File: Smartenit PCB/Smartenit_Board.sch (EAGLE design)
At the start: 86 parts, among them J3 2X5CONNECTOR1.27MM, Q1 QUARTZ_3.58M_2PIN, U1 ADE7953, U2 ESP-WROOM-32, U3 SN74LVC1G3157

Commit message: renumber board
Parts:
- removed D6: (no value), SparkFun:DIODESMA
- removed R43: 470, Nizanlib:0402-RES
- added D3: 250mA/100V, SparkFun-DiscreteSemi:DIODE-BAS16J
- added R37: 124k, SparkFun-Resistors:100KOHM-0603-1/10W-1%
- C1: value 20p -> 105/25V; device Nizanlib:0402-CAP -> SparkFun-Capacitors:680PF-0603-50V-10%
- C11, C12: value 333n -> 475n
- C14: value 475n -> 333n
- C15: value 104n -> 475n
- C16: value 475n -> 104n
- C17: device resistor:C-EUC0805K -> Nizanlib:0402-CAP
- C18: value 104 -> 333n; device SparkFun-Capacitors:680PF-0603-50V-10% -> Nizanlib:0402-CAP
- C19: value 22uF/6.3V -> 333n; device SparkFun-Capacitors:680PF-0603-50V-10% -> resistor:C-EUC0805K
- C2: value 20p -> 10uF/6.3V; device Nizanlib:0402-CAP -> SparkFun:CAP0603-CAP
- C20: value 104 -> 333n; device SparkFun-Capacitors:680PF-0603-50V-10% -> resistor:C-EUC0805K
- C21: value 150p -> 104; device SparkFun-Capacitors:680PF-0603-50V-10% -> SparkFun:CAP0603-CAP
- C22: value 105/25V -> (none); device SparkFun-Capacitors:680PF-0603-50V-10% -> SparkFun:CAP_POL1206
- C23: value 10uF/6.3V -> 104; device SparkFun:CAP0603-CAP -> SparkFun-Capacitors:680PF-0603-50V-10%
- C24: value 104 -> (none); device Nizanlib:0402-CAP -> SparkFun:CAP_POLPTH1
- C25: device SparkFun:CAP0603-CAP -> SparkFun-Capacitors:680PF-0603-50V-10%
- C26: value (none) -> 150p; device SparkFun:CAP_POLPTH1 -> SparkFun-Capacitors:680PF-0603-50V-10%
- C3: value 104n -> 104
- C4: value 104n -> 333n
- C5: value 333n -> 104n
- C6: value 333n -> 22uF/6.3V; device Nizanlib:0402-CAP -> SparkFun-Capacitors:680PF-0603-50V-10%
- C7: value 333n -> 20p; device resistor:C-EUC0805K -> Nizanlib:0402-CAP
- C8: value 475n -> 20p
- C9: value (none) -> 104n; device SparkFun:CAP_POL1206 -> Nizanlib:0402-CAP
- D1: value 250mA/100V -> (none); device SparkFun-DiscreteSemi:DIODE-BAS16J -> SparkFun:DIODESMA
- R1, R10: value 1k -> 10k; device Nizanlib:0402-RES -> SparkFun-Resistors:100KOHM-0603-1/10W-1%
- R11: value 51 -> 10k; device Nizanlib:0402-RES -> SparkFun-Resistors:100KOHM-0603-1/10W-1%
- R12: value 9.1k -> 4.7k; device Nizanlib:0402-RES -> SparkFun-Resistors:100KOHM-0603-1/10W-1%
- R13: value 100k -> 1k; device SparkFun-Resistors:100KOHM-0603-1/10W-1% -> SparkFun-Resistors:1KOHM-0603-1/10W-1%
- R14, R15: value 100k -> 470; device SparkFun-Resistors:100KOHM-0603-1/10W-1% -> Nizanlib:0402-RES
- R16: value 124k -> 12k; device SparkFun-Resistors:100KOHM-0603-1/10W-1% -> Nizanlib:0402-RES
- R17: value 40.2k -> 1k; device SparkFun-Resistors:100KOHM-0603-1/10W-1% -> Nizanlib:0402-RES
- R18: value 1k -> 9.1k; device resistor:R-EU_ -> Nizanlib:0402-RES
- R19: value 1k -> 51; device resistor:R-EU_ -> Nizanlib:0402-RES
- R2: value 1k -> 56k; device Nizanlib:0402-RES -> SparkFun-Resistors:100KOHM-0603-1/10W-1%
- R20: value 100k -> 51; device SparkFun-Resistors:100KOHM-0603-1/10W-1% -> Nizanlib:0402-RES
- R21: value 10k -> 1k; device SparkFun-Resistors:10KOHM-0603-1/10W-1% -> Nizanlib:0402-RES
- R22: value 9.1k -> 10k
- R23: value 220 -> 1k; device SparkFun-Resistors:10KOHM-0603-1/10W-1% -> resistor:R-EU_
- R24: value 220 -> 1k; device SparkFun-Resistors:10KOHM-0603-1/10W-1% -> Nizanlib:0402-RES
- R25: value 220 -> 9.1k; device SparkFun-Resistors:10KOHM-0603-1/10W-1% -> Nizanlib:0402-RES
- R26: value 10k -> 1k; device SparkFun-Resistors:100KOHM-0603-1/10W-1% -> Nizanlib:0402-RES
- R27: value 4.7k -> 9.1k; device SparkFun-Resistors:100KOHM-0603-1/10W-1% -> Nizanlib:0402-RES
- R28: value 10k -> 9.1k; device SparkFun-Resistors:100KOHM-0603-1/10W-1% -> Nizanlib:0402-RES
- R29: value 4.7k -> 51; device SparkFun-Resistors:100KOHM-0603-1/10W-1% -> Nizanlib:0402-RES
- R3: value 10k -> 200k; device Nizanlib:0402-RES -> SparkFun-Resistors:100KOHM-0603-1/10W-1%
- R30: value 10k -> 51; device SparkFun-Resistors:100KOHM-0603-1/10W-1% -> Nizanlib:0402-RES
- R31: device SparkFun-Resistors:100KOHM-0603-1/10W-1% -> resistor:R-EU_
- R32: value 200k -> 12k; device SparkFun-Resistors:100KOHM-0603-1/10W-1% -> Nizanlib:0402-RES
- R33: value 56k -> 220; device SparkFun-Resistors:100KOHM-0603-1/10W-1% -> SparkFun-Resistors:10KOHM-0603-1/10W-1%
- R34: value 1k -> 100k; device SparkFun-Resistors:1KOHM-0603-1/10W-1% -> SparkFun-Resistors:100KOHM-0603-1/10W-1%
- R35: value 1k -> 40.2k; device SparkFun-Resistors:1KOHM-0603-1/10W-1% -> SparkFun-Resistors:100KOHM-0603-1/10W-1%
- R36, R40: value 12k -> 100k; device Nizanlib:0402-RES -> SparkFun-Resistors:100KOHM-0603-1/10W-1%
- R38: value 470 -> 10k; device Nizanlib:0402-RES -> SparkFun-Resistors:10KOHM-0603-1/10W-1%
- R39: value 470 -> 100k; device Nizanlib:0402-RES -> SparkFun-Resistors:100KOHM-0603-1/10W-1%
- R4: value 9.1k -> 1k; device Nizanlib:0402-RES -> SparkFun-Resistors:1KOHM-0603-1/10W-1%
- R41: value 470 -> 220; device Nizanlib:0402-RES -> SparkFun-Resistors:10KOHM-0603-1/10W-1%
- R42: value 12k -> 220; device Nizanlib:0402-RES -> SparkFun-Resistors:10KOHM-0603-1/10W-1%
- R5: value 51 -> 470
- R6: value 51 -> 12k
- R7: value 9.1k -> 470
- R8: device Nizanlib:0402-RES -> SparkFun-Resistors:100KOHM-0603-1/10W-1%
- R9: value 51 -> 4.7k; device Nizanlib:0402-RES -> SparkFun-Resistors:100KOHM-0603-1/10W-1%
- U$1: value MP1584 -> DMC3400SSDW; device Smart_Charger:MP1584 -> Smart_Charger:DMC3400SSDW
- U$3: value DMC3400SSDW -> 2MM_CONN8; device Smart_Charger:DMC3400SSDW -> Smart_Charger:2MM_CONN8
- U$4: value 2MM_CONN8 -> MP1584; device Smart_Charger:2MM_CONN8 -> Smart_Charger:MP1584
- U1: value ADE7953 -> SN74LVC1G3157; device CalPlug:ADE7953 -> Smart_Charger:SN74LVC1G3157
- U2: value ESP-WROOM-32 -> ADE7953; device esp32:ESP-WROOM-32 -> CalPlug:ADE7953
- U3: value SN74LVC1G3157 -> ESP-WROOM-32; device Smart_Charger:SN74LVC1G3157 -> esp32:ESP-WROOM-32
- renumbered D5 to D2, J3 to J1, LD1 to LD100, LED1 to LED100, S1 to S100
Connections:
- net -12V: now also C1.2, R12.1, U$2.S1; no longer C22.2, R29.1, U$3.S1
- net 12V: now also C23.2, C24.+, R40.2, R9.1, U$2.S2, U$4.VEN; no longer C20.2, C26.+, R14.2, R27.1, U$1.VEN, U$3.S2
- net 3.3V: now also C2.1, C21.1, C22.+, C5.2, C6.2, C9.2, R1.1, R15.1, R22.1, R37.2, R38.2, R6.2, U$1.S2, U1.VCC, U2.PULL_HIGH1, U2.PULL_HIGH2, U2.VDD, U3.3V3; no longer C19.2, C23.1, C25.1, C3.2, C4.2, C9.+, R21.2, R26.1, R3.1, R40.2, R42.2, R43.1, U$2.S2, U1.PULL_HIGH1, U1.PULL_HIGH2, U1.VDD, U2.3V3, U3.VCC
- net ADC1: now also R2.2, R3.1, U3.IO13; no longer R32.1, R33.2, U2.IO13
- net DIO0: now also U2.CS, U3.IO14; no longer U1.CS, U2.IO14
- net DIO1: now also U1.S, U3.IO27; no longer U2.IO27, U3.S
- net DIO10: now also U3.IO35; no longer U2.IO35
- net DIO11: now also U3.IO32; no longer U2.IO32
- net DIO12: now also U3.IO33; no longer U2.IO33
- net DIO13: now also R1.2, U$1.G1, U$1.G2, U3.IO25; no longer R26.2, U$2.G1, U$2.G2, U2.IO25
- net DIO16: now also R41.1, U3.IO18; no longer R24.1, U2.IO18
- net DIO17: now also R42.1, U3.IO19; no longer R25.1, U2.IO19
- net DIO5: now also R22.2, U2./IRQ, U3.IO26; no longer R3.2, U1./IRQ, U2.IO26
- net DIO8: now also R38.1, U3.IO16; no longer R21.1, U2.IO16
- net DIO9: now also R33.1, U3.IO17; no longer R23.1, U2.IO17
- net GND: now also C11.2, C12.1, C14.2, C17.1, C18.2, C19.2, C2.2, C20.2, C21.2, C22.-, C23.1, C24.-, C6.1, C7.1, C8.1, C9.1, D3.A, R17.2, R2.1, R20.1, R21.1, R23.2, R24.2, R26.1, R29.1, R30.2, R31.2, R32.1, R34.1, R35.1, U$1.S1, U$3.7, U$4.GND, U1.GND, U2.AGND, U2.DGND, U2.PAD, U2.PULL_LOW, U3.GND@1, U3.GND@15, U3.GND@38; no longer C11.1, C12.2, C14.1, C17.2, C19.1, C2.1, C20.1, C22.1, C23.2, C24.1, C25.2, C26.-, C6.2, C7.2, C8.2, C9.-, D6.A, R1.1, R10.2, R11.2, R13.1, R15.1, R17.1, R18.2, R2.2, R33.1, R5.1, R6.2, R8.1, R9.1, U$1.GND, U$2.S1, U$4.7, U1.AGND, U1.DGND, U1.PAD, U1.PULL_LOW, U2.GND, U2.GND@1, U2.GND@15, U2.GND@38
- net GPIO0: now also R14.1, R16.1, U3.IO0; no longer R41.1, R42.1, U2.IO0
- net IAN: now also R27.1, R30.1, U$3.2; no longer R11.1, R22.1, U$4.2
- net IAP: now also R28.1, R29.2, U$3.1; no longer R4.1, R9.2, U$4.1
- net IBN: now also R18.1, R19.1, U$3.4; no longer R6.1, R7.1, U$4.4
- net IBP: now also R20.2, R25.1, U$3.3; no longer R12.1, R5.2, U$4.3
- net LNV1: now also R4.1, U$3.5; no longer R35.1, U$4.5
- net LNV2: now also R13.1, U$3.6; no longer R34.1, U$4.6
- net N$1: now also C7.2, U2.CLKOUT; no longer C1.2, U1.CLKOUT
- net N$10: now also C18.1, U2.I1N; no longer C12.1, U1.I1N
- net N$11: now also R18.2, R24.1; no longer R10.1, R7.2
- net N$12: now also U2.VINTD; no longer U1.VINTD
- net N$13: now also C14.1, U2.I2N; no longer C6.1, U1.I2N
- net N$14: now also R40.1, U$4.EN; no longer R14.1, U$1.EN
- net N$15: now also C26.2, U$4.COMP; no longer C21.2, U$1.COMP
- net N$17: now also C26.1, R34.2; no longer C21.1, R15.2
- net N$18: now also C25.2, D3.C, U$4.SW; no longer C18.2, D1.C, U$1.SW
- net N$19: now also R35.2, R37.1, U$4.FB; no longer R16.1, R17.2, U$1.FB
- net N$2: now also C8.2, U2.CLKIN; no longer C2.2, U1.CLKIN
- net N$20: now also R39.1; no longer R20.1
- net N$21: now also R33.2; no longer R23.2
- net N$22: now also C25.1, U$4.BST; no longer C18.1, U$1.BST
- net N$23: now also R11.2, R9.2, U$2.G2; no longer R27.2, R30.2, U$3.G2
- net N$24: now also C17.2, R26.2, R28.2, U2.I1P; no longer C11.2, R1.2, R4.2, U1.I1P
- net N$25: now also R41.2; no longer R24.2
- net N$26: now also R42.2; no longer R25.2
- net N$27: now also R17.1, R27.2; no longer R2.1, R22.2
- net N$28: now also R10.1, U$1.D2; no longer R28.1, U$2.D2
- net N$29: now also R10.2, R12.2, U$2.G1; no longer R28.2, R29.2, U$3.G1
- net N$3: now also C20.1, R23.1, U1.A, U2.VN; no longer C7.1, R19.1, U1.VN, U3.A
- net N$30: now also R15.2, U3.IO2; no longer R43.2, U2.IO2
- net N$32: now also R11.1, U$1.D1; no longer R30.1, U$2.D1
- net N$33: now also R8.1, U$2.D1, U$2.D2; no longer R31.1, U$3.D1, U$3.D2
- net N$38: now also R39.2; no longer R20.2
- net N$4: now also R36.2, U$4.FREQ; no longer R13.2, U$1.FREQ
- net N$40: now also R14.2; no longer R41.2
- net N$45: now also U3.IO34; no longer U2.IO34
- net N$46: now also U3.SENSOR_VN; no longer U2.SENSOR_VN
- net N$47: now also U3.SENSOR_VP; no longer U2.SENSOR_VP
- net N$5: now also C4.2, R21.2, R25.2, U2.I2P; no longer C5.2, R12.2, R8.2, U1.I2P
- net N$53: now also U3.IO21; no longer U2.IO21
- net N$54: now also R13.2, U1.B2; no longer R34.2, U3.B2
- net N$55: now also R4.2, U1.B1; no longer R35.2, U3.B1
- net N$62: now also R5.1; no longer R39.1
- net N$65: now also R7.1; no longer R38.1
- net N$7: now also C11.1, U2.REF; no longer C8.1, U1.REF
- net N$8: now also C12.2, U2.VINTA; no longer C14.2, U1.VINTA
- net NRST: now also C3.2, R5.2, R6.1, U3.EN; no longer C24.2, R39.2, R40.1, U2.EN
- net PILOT: now also D1.C, R3.2, R8.2, U$3.8; no longer D6.C, R31.2, R32.2, U$4.8
- net RESET_ISO: now also U2.RESET, U3.IO12; no longer U1.RESET, U2.IO12
- net RXD0: now also R7.2, U3.RXD0; no longer R38.2, U2.RXD0
- net SPIMISO: now also U2.MISO, U3.SDO; no longer U1.MISO, U2.SDO
- net SPIMOSI: now also U2.MOSI, U3.SD1; no longer U1.MOSI, U2.SD1
- net SPISCLK: now also U2.SCLK, U3.CLK; no longer U1.SCLK, U2.CLK
- net SS: now also R32.2, U3.IO15; no longer R36.2, U2.IO15
- net TXD0: now also U3.TXD0; no longer U2.TXD0
- net V2P: now also C19.1, R31.1, U2.VP; no longer C17.1, R18.1, U1.VP
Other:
- moved on the sheet: C1, C11, C12, C14, C15, C16, C17, C18, C19, C2, C20, C21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

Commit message: Fixed Silk Screen final before sending to Al
fixed silk screen and renumbered parts
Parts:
- removed LD100: (no value), led:DUOLED-RG-A
- removed LED100: (no value), SparkFun:LED3MM
- added BLUE_LED: (no value), SparkFun:LED3MM
- added R/G_LED: (no value), led:DUOLED-RG-A
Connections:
- net ADC1 renamed PILOT_READ
- net DIO0 renamed CS
- net DIO1 renamed MPLEX
- net DIO10 renamed GFI_TEST
- net DIO13 renamed PILOT_GEN
- net DIO16 renamed GREEN_LED
- net DIO17 renamed RED_LED
- net DIO8 renamed BUTTON
- net DIO9 renamed BLUE_LED
- net N$30 renamed GPIO2
- net 3.3V: now also BLUE_LED.A, R/G_LED.A; no longer LD100.A, LED100.A, R15.1
- net GND: now also R15.1
- net N$21: now also BLUE_LED.C; no longer LED100.C
- net N$25: now also R/G_LED.CG; no longer LD100.CG
- net N$26: now also R/G_LED.CR; no longer LD100.CR
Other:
- moved on the sheet: C2, C21, C23, C24, C25, C26, C3, C6, D3, L1, R14, R15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

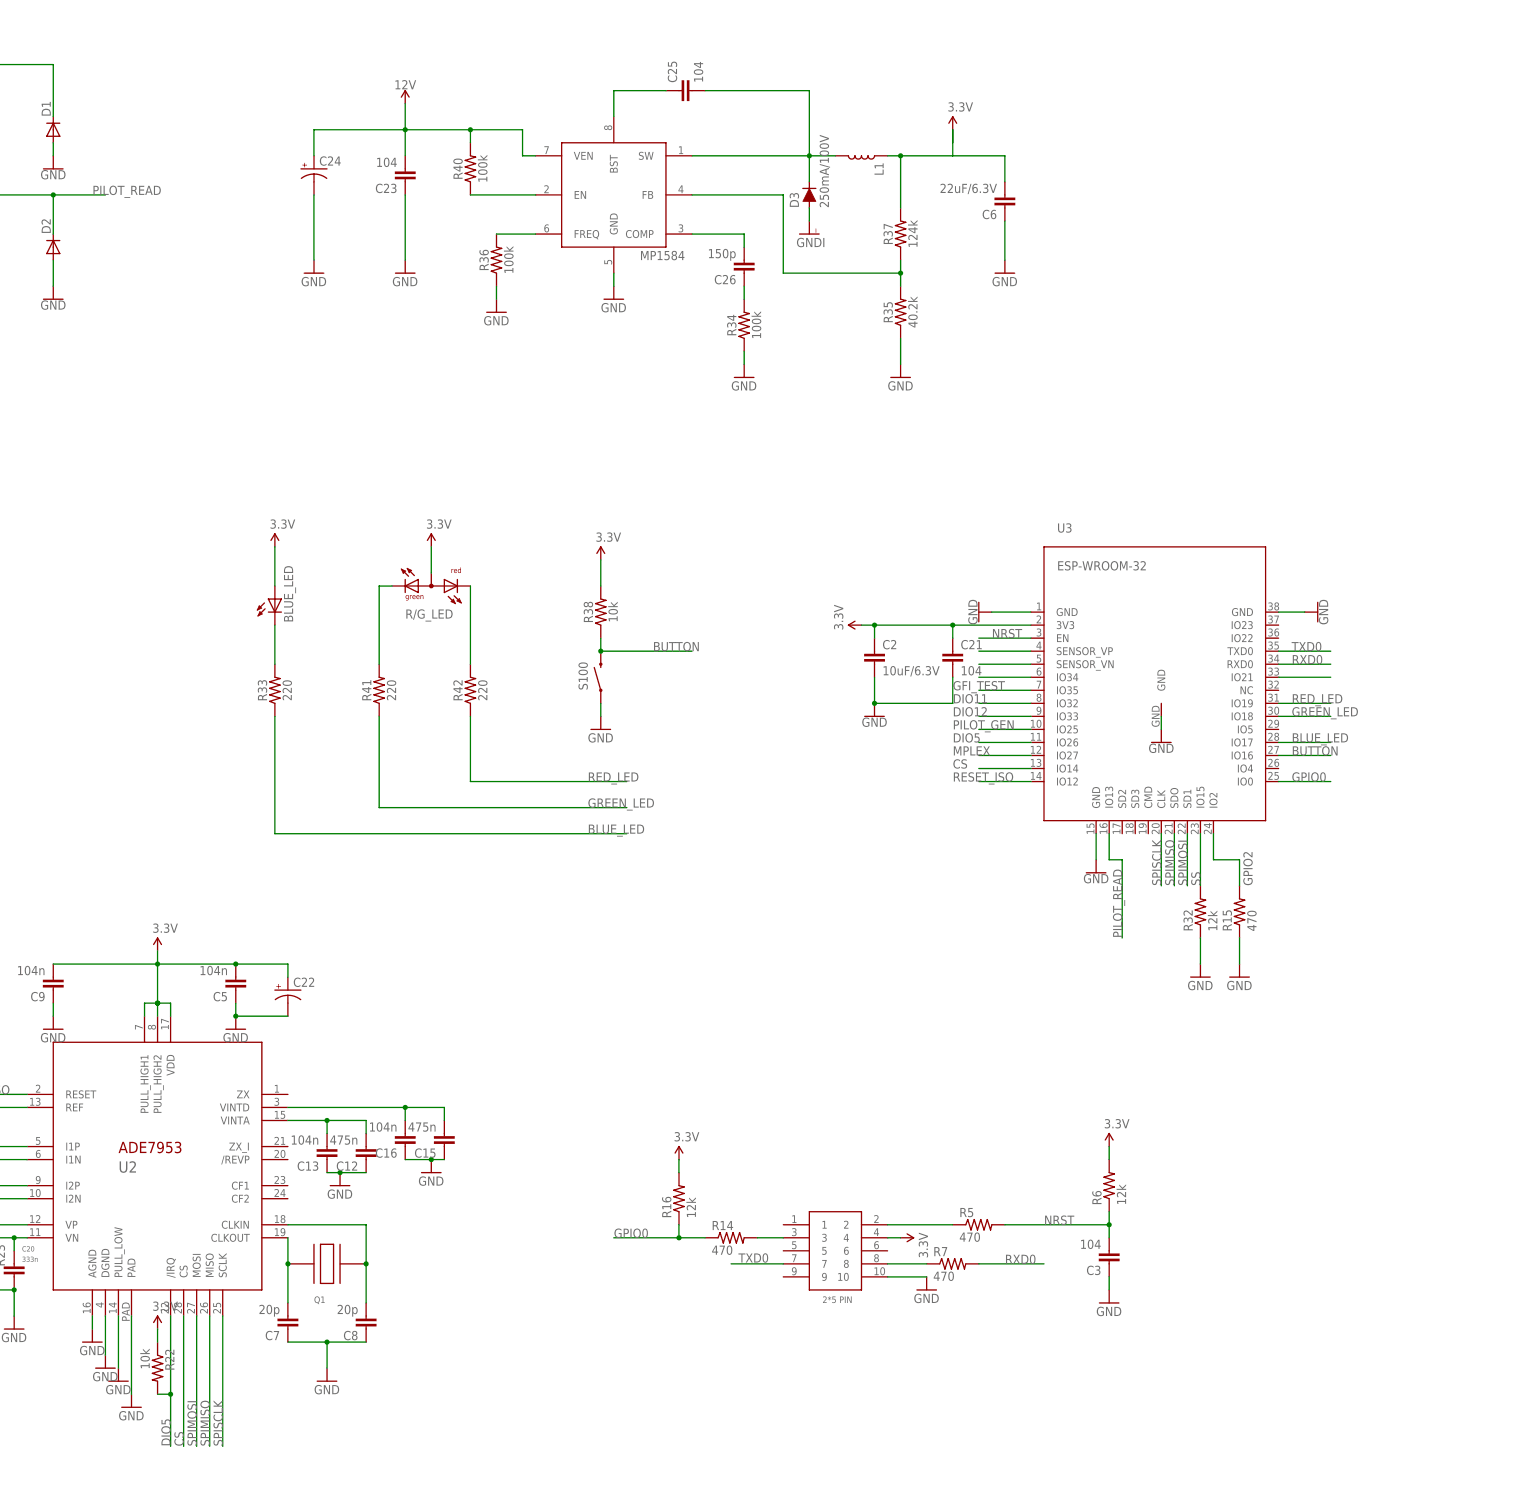
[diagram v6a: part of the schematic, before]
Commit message: Changed ground planes
separated into analog and digital grounds. Rearachnged layout for better coupling.
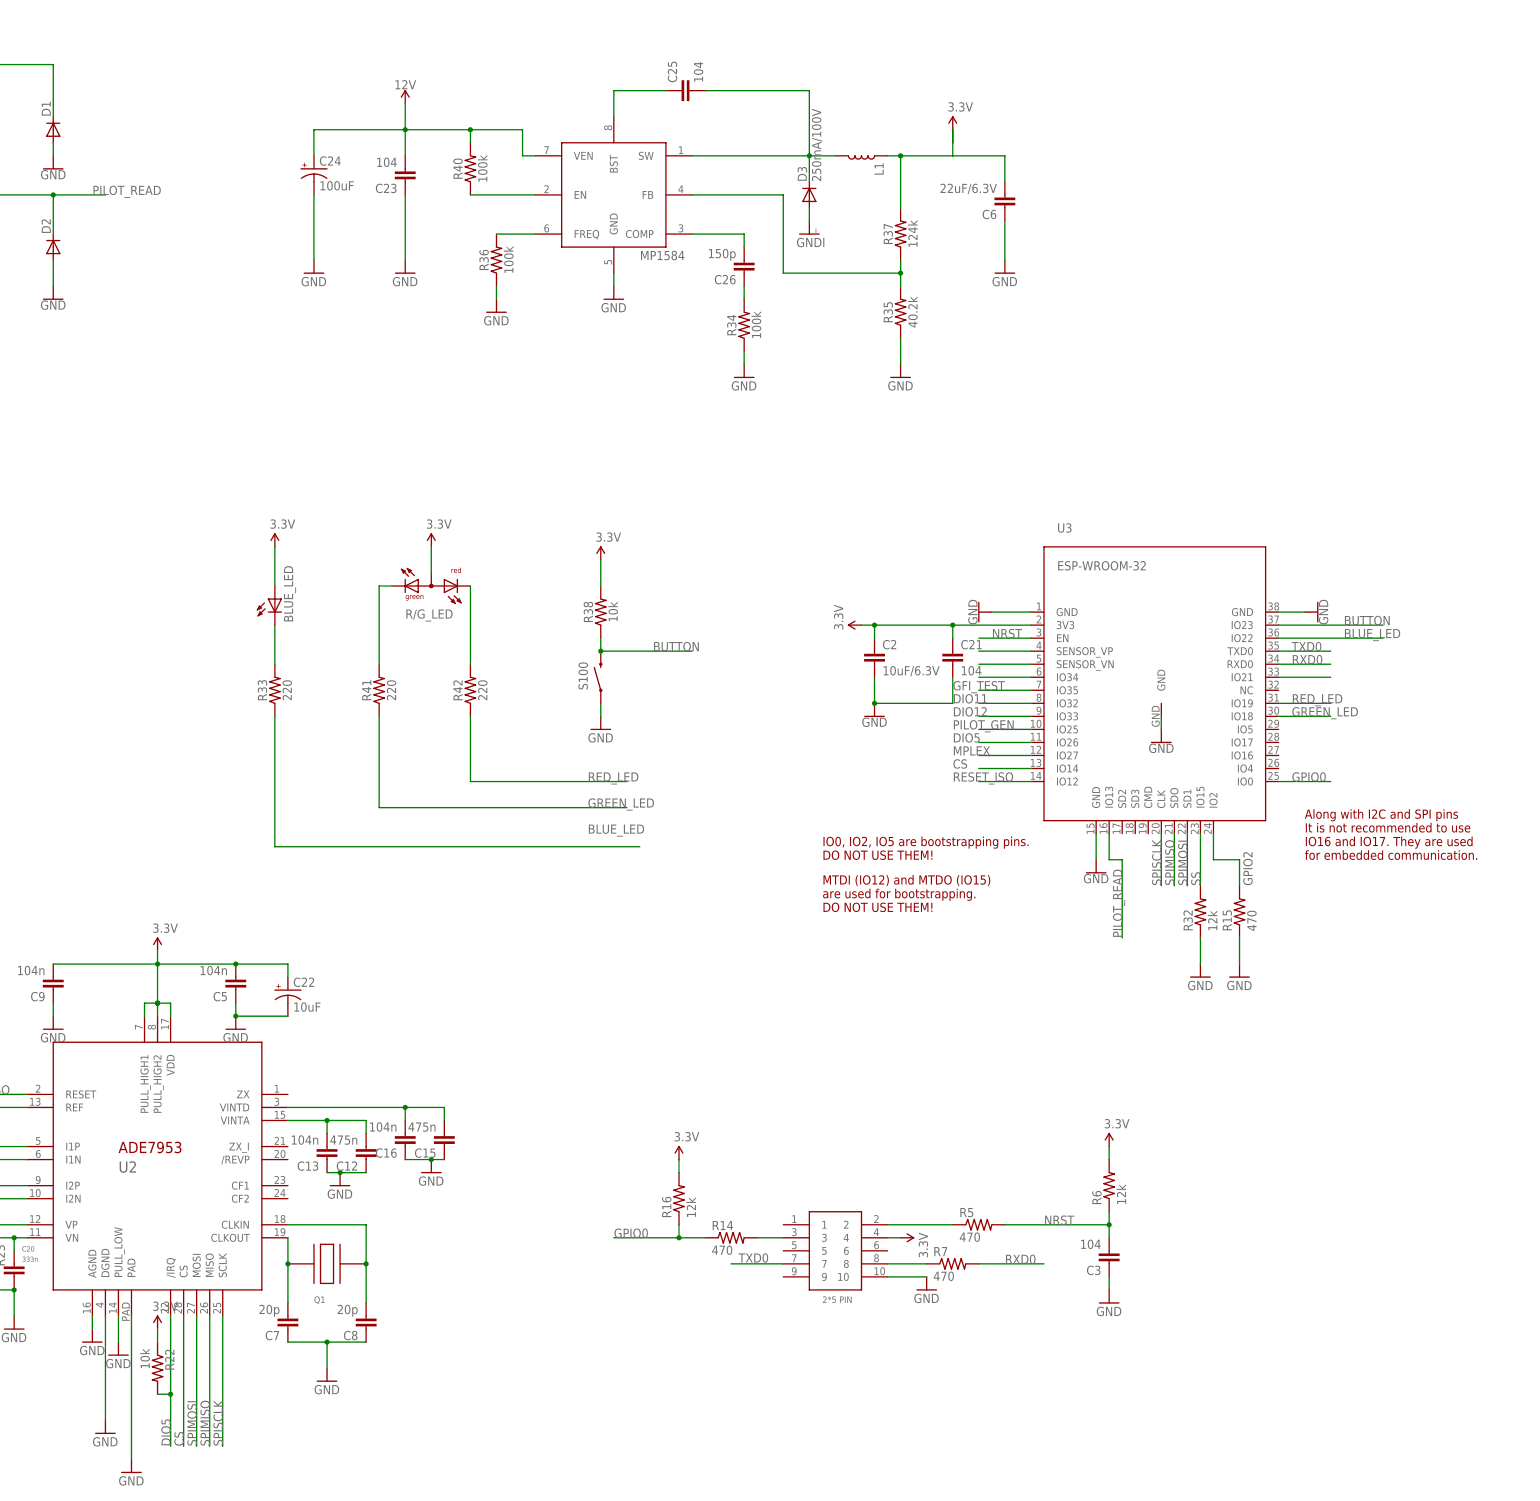
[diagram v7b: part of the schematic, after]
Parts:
- C22: value (none) -> 10uF
- C24: value (none) -> 100uF
- D2: device SparkFun:DIODEHV -> SparkFun:DIODESOD
- D3: device SparkFun-DiscreteSemi:DIODE-BAS16J -> diode:DIODE-DO214BA
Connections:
- removed net GND: C1.1, C10.2, C11.2, C12.1, C13.1, C14.2, C15.1, C16.1, C17.1, C18.2, C19.2, C2.2, C20.2, C21.2, C22.-, C23.1, C24.-, C3.1, C4.1, C5.1, C6.1, C7.1, C8.1, C9.1, D1.A, D2.A, D3.A, J1.10, R15.1, R17.2, R19.2, R2.1, R20.1, R21.1, R23.2, R24.2, R26.1, R29.1, R30.2, R31.2, R32.1, R34.1, R35.1, R36.1, S100.1, U$1.S1, U$3.7, U$4.GND, U$5.PIN5, U1.GND, U2.AGND, U2.DGND, U2.PAD, U2.PULL_LOW, U3.GND, U3.GND@1, U3.GND@15, U3.GND@38
- new net AGND: C1.1, C10.2, C11.2, C14.2, C17.1, C18.2, C19.2, C2.2, C20.2, C21.2, C22.-, C23.1, C24.-, C4.1, C5.1, C6.1, C7.1, C8.1, C9.1, D2.A, D3.A, R17.2, R19.2, R2.1, R20.1, R21.1, R23.2, R24.2, R26.1, R29.1, R30.2, R31.2, U$3.7, U$5.PIN5, U1.GND, U2.AGND, U2.PAD, U2.PULL_LOW, U3.GND, U3.GND@15
- new net DGND: C12.1, C13.1, C15.1, C16.1, C3.1, D1.A, J1.10, R15.1, R32.1, R34.1, R35.1, R36.1, S100.1, U$1.S1, U$4.GND, U2.DGND, U3.GND@1, U3.GND@38
- net BLUE_LED: now also U3.IO22; no longer U3.IO17
- net BUTTON: now also U3.IO23; no longer U3.IO16
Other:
- note added: "Along with I2C and SPI pins It is not recommended to use IO16 and IO17. They are used for embedded communication."
- note added: "IO0, IO2, IO5 are bootstrapping pins. DO NOT USE THEM!"
- note added: "MTDI (IO12) and MTDO (IO15) are used for bootstrapping. DO NOT USE THEM!"
